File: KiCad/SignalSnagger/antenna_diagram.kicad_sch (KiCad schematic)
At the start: 0 parts

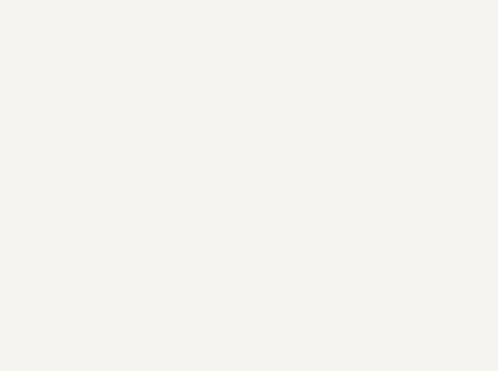
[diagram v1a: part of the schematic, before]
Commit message: PCB Layout
Most 3D models have been included in the schematic
PCB layout places all tall parts on the back of the board
Added knob to BOM
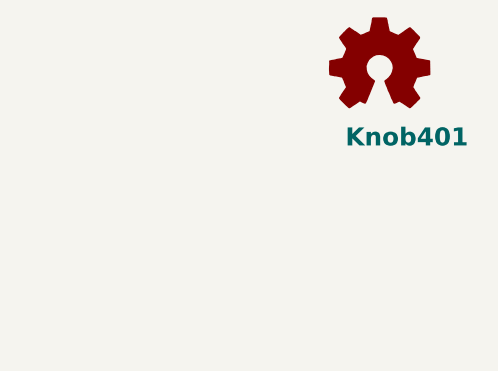
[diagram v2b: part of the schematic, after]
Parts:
- added Knob401: Logo_Open_Hardware_Small, symbol Graphic:Logo_Open_Hardware_Small
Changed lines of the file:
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@@
   (title_block
     (title "SignalSnagger")
-    (date "2024-04-01")
-    (rev "0.315")
+    (date "2024-04-11")
+    (rev "0.316")
   )
   (image (at 74.93 96.52) (scale 0.712458)
@@
     (effects (font (size 1.27 1.27)) (justify left bottom))
   )
+  (symbol (lib_id "Graphic:Logo_Open_Hardware_Small") (at 168.91 46.99 0) (unit 1)
+    (in_bom yes) (on_board yes)
+    (property "Reference" "Knob401" (id 0) (at 165.1 54.61 0)
+      (effects (font (size 2 2) bold) (justify left))
+    )
+    (property "Value" "Logo_Open_Hardware_Small" (id 1) (at 168.91 52.705 0)
+      (effects (font (size 1.27 1.27)) hide)
+    )
+    (property "Footprint" "" (id 2) (at 168.91 46.99 0)
+      (effects (font (size 1.27 1.27)) hide)
+    )
+    (property "Datasheet" "~" (id 3) (at 168.91 46.99 0)
+      (effects (font (size 1.27 1.27)) hide)
+    )
+    (property "Link" "https://www.adafruit.com/product/5527" (id 4) (at 168.91 46.99 0)
+      (effects (font (size 1.27 1.27)) hide)
+    )
+  )
 )

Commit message: Removed spare sense switches
Updated schematic and PCB to remove spare sense switches.
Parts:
- Knob401: value Logo_Open_Hardware_Small -> (none)
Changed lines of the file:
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@@
       (effects (font (size 2 2) bold) (justify left))
     )
-    (property "Value" "Logo_Open_Hardware_Small" (id 1) (at 168.91 52.705 0)
+    (property "Value" "" (id 1) (at 168.91 52.705 0)
       (effects (font (size 1.27 1.27)) hide)
     )

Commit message: BOM Updates
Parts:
- Knob401: value (none) -> Logo_Open_Hardware_Small; footprint (none) -> Oddities:Dummy_Empty
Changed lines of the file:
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@@
       (effects (font (size 2 2) bold) (justify left))
     )
-    (property "Value" "" (id 1) (at 168.91 52.705 0)
+    (property "Value" "Logo_Open_Hardware_Small" (id 1) (at 168.91 52.705 0)
       (effects (font (size 1.27 1.27)) hide)
     )
-    (property "Footprint" "" (id 2) (at 168.91 46.99 0)
+    (property "Footprint" "Oddities:Dummy_Empty" (id 2) (at 168.91 46.99 0)
       (effects (font (size 1.27 1.27)) hide)
     )
